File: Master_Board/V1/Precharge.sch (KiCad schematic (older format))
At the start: 24 parts, among them J701 649002227222, J702 649002227222, Q701 BC849BLT1G, Q702 BC849BLT1G, U701 LTV-816S, U702 LTV-816S

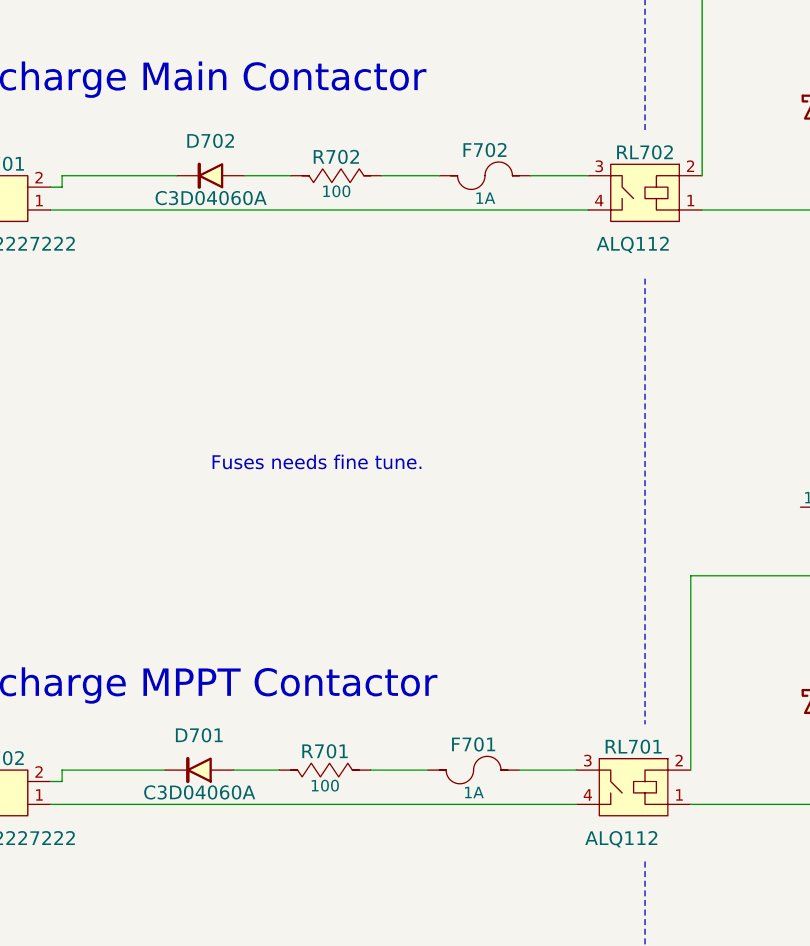
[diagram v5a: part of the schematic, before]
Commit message: Create Master board PCB
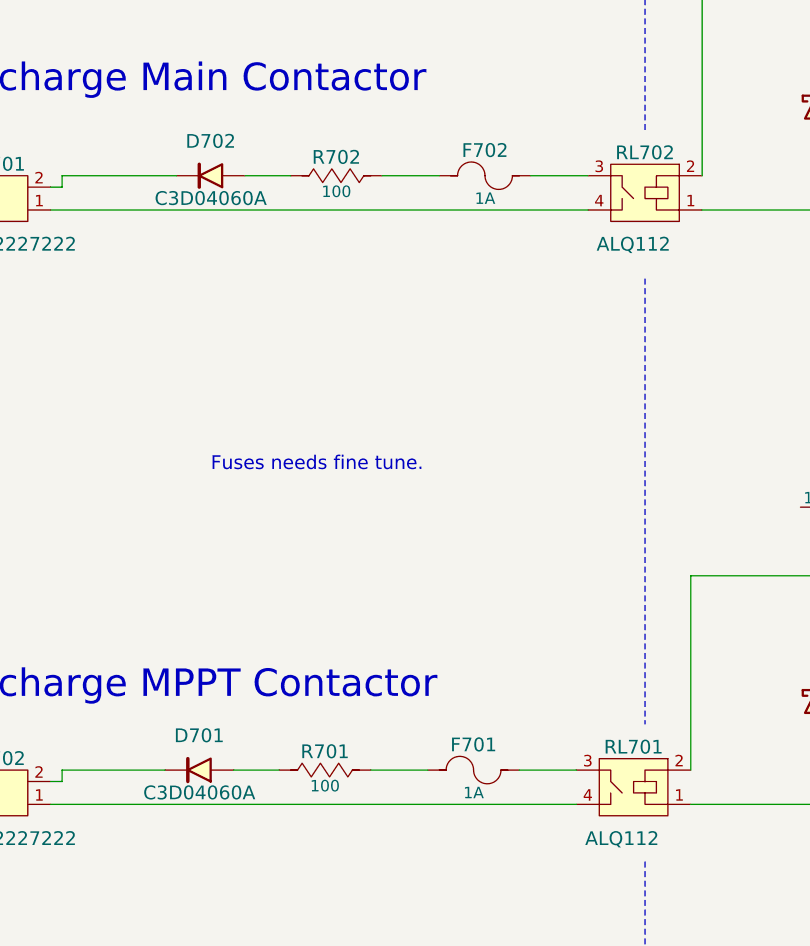
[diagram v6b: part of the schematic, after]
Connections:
- net at RL702.3: now also F702.2; no longer F702.1
- net at R702.1: now also D702.2 (Anode); no longer F702.2
- net at R702.2: now also F702.1; no longer D702.2 (Anode)
- net at RL701.3: now also F701.2; no longer F701.1
- net at R701.1: now also D701.2 (Anode); no longer F701.2
- net at R701.2: now also F701.1; no longer D701.2 (Anode)
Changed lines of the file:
@@
 	5300 4600 5300 4550
-$Comp
-L 39511000440 F702
-U 1 1 5945789A
-P 3050 2350
-F 0 "F702" H 3050 2460 60  0000 C CNN
-F 1 "39511000440" H 3050 2050 50  0001 C CNN
-F 2 "Fuses:TE5_395" H 3050 1450 30  0001 C CNN
-F 3 "http://www.littelfuse.com/~/media/electronics/datasheets/fuses/littelfuse_fuse_395_datasheet.pdf.pdf" H 3050 1400 30  0001 C CNN
-F 4 "Digikey" H 3050 1150 60  0001 C CNN "Supplier"
-F 5 "WK0009-ND" H 3050 1050 60  0001 C CNN "Supplier Part Number"
-F 6 "Littelfuse Inc." H 3050 900 60  0001 C CNN "Manufacturer"
-F 7 "56200001009" H 3050 750 60  0001 C CNN "Manufacturer Part Number"
-F 8 "FUSE HOLDER RADIAL 250V 6.3A PCB" H 3050 600 60  0001 C CNN "Description"
-F 9 "1A" H 3050 2250 50  0000 C CNN "Current Rating (A)"
-F 10 "-" H 2950 2150 50  0001 C CNN "Voltage Rating - DC"
-F 11 "125V" H 3150 2150 60  0001 C CNN "Voltage Rating - AC"
-F 12 "Fuse Holder" H 3050 1250 60  0001 C CNN "Fuse Holder"
-	1    3050 2350
-	-1   0    0    -1
-$EndComp
 $Comp
 L 649002227222 J701
@@
 Wire Wire Line
 	3500 2350 3250 2350
-$Comp
-L TR50JBC100R R702
-U 1 1 59458C40
-P 2400 2350
-F 0 "R702" H 2400 2430 60  0000 C CNN
-F 1 "TR50JBC100R" H 2400 2050 50  0001 C CNN
-F 2 "Resistors:TR50" H 2400 1450 30  0001 C CNN
-F 3 "https://www.seielect.com/Catalog/SEI-tr.pdf" H 2400 1400 30  0001 C CNN
-F 4 "Digikey" H 2400 1950 60  0001 C CNN "Supplier"
-F 5 "TR50JBC100R-ND" H 2400 1850 60  0001 C CNN "Supplier Part Number"
-F 6 "Stackpole Electronics Inc." H 2400 1750 60  0001 C CNN "Manufacturer"
-F 7 "TR50JBC100R" H 2400 1650 60  0001 C CNN "Manufacturer Part Number"
-F 8 "RES 100 OHM 50W 5% TO220" H 2400 1550 60  0001 C CNN "Description"
-F 9 "100" H 2400 2280 50  0000 C CNN "Resistance (Ohms)"
-F 10 "±5%" H 2810 2270 50  0001 C CNN "Tolerance (%)"
-F 11 "50W" H 2400 2210 50  0001 C CNN "Puissance (Watts)"
-	1    2400 2350
-	-1   0    0    -1
-$EndComp
 Wire Wire Line
 	2850 2350 2600 2350
 Wire Wire Line
 	2200 2350 2000 2350
-$Comp
-L 39511000440 F701
-U 1 1 59458F9F
-P 3000 4950
-F 0 "F701" H 3000 5060 60  0000 C CNN
-F 1 "39511000440" H 3000 4650 50  0001 C CNN
-F 2 "Fuses:TE5_395" H 3000 4050 30  0001 C CNN
-F 3 "http://www.littelfuse.com/~/media/electronics/datasheets/fuses/littelfuse_fuse_395_datasheet.pdf.pdf" H 3000 4000 30  0001 C CNN
-F 4 "Digikey" H 3000 3750 60  0001 C CNN "Supplier"
-F 5 "WK0009-ND" H 3000 3650 60  0001 C CNN "Supplier Part Number"
-F 6 "Littelfuse Inc." H 3000 3500 60  0001 C CNN "Manufacturer"
-F 7 "56200001009" H 3000 3350 60  0001 C CNN "Manufacturer Part Number"
-F 8 "FUSE HOLDER RADIAL 250V 6.3A PCB" H 3000 3200 60  0001 C CNN "Description"
-F 9 "1A" H 3000 4850 50  0000 C CNN "Current Rating (A)"
-F 10 "-" H 2900 4750 50  0001 C CNN "Voltage Rating - DC"
-F 11 "125V" H 3100 4750 60  0001 C CNN "Voltage Rating - AC"
-F 12 "Fuse Holder" H 3000 3850 60  0001 C CNN "Fuse Holder"
-	1    3000 4950
-	-1   0    0    -1
-$EndComp
 $Comp
 L 649002227222 J702
@@
 Wire Wire Line
 	3450 4950 3200 4950
-$Comp
-L TR50JBC100R R701
-U 1 1 59458FBA
-P 2350 4950
-F 0 "R701" H 2350 5030 60  0000 C CNN
-F 1 "TR50JBC100R" H 2350 4650 50  0001 C CNN
-F 2 "Resistors:TR50" H 2350 4050 30  0001 C CNN
-F 3 "https://www.seielect.com/Catalog/SEI-tr.pdf" H 2350 4000 30  0001 C CNN
-F 4 "Digikey" H 2350 4550 60  0001 C CNN "Supplier"
-F 5 "TR50JBC100R-ND" H 2350 4450 60  0001 C CNN "Supplier Part Number"
-F 6 "Stackpole Electronics Inc." H 2350 4350 60  0001 C CNN "Manufacturer"
-F 7 "TR50JBC100R" H 2350 4250 60  0001 C CNN "Manufacturer Part Number"
-F 8 "RES 100 OHM 50W 5% TO220" H 2350 4150 60  0001 C CNN "Description"
-F 9 "100" H 2350 4880 50  0000 C CNN "Resistance (Ohms)"
-F 10 "±5%" H 2760 4870 50  0001 C CNN "Tolerance (%)"
-F 11 "50W" H 2350 4810 50  0001 C CNN "Puissance (Watts)"
-	1    2350 4950
-	-1   0    0    -1
-$EndComp
 Wire Wire Line
 	2800 4950 2550 4950
@@
 	-1   0    0    -1
 $EndComp
+$Comp
+L 39511000440 F701
+U 1 1 59621787
+P 3000 4950
+F 0 "F701" H 3000 5060 60  0000 C CNN
+F 1 "39511000440" H 3000 4650 50  0001 C CNN
+F 2 "Fuses:TE5_395" H 3000 4050 30  0001 C CNN
+F 3 "http://www.littelfuse.com/~/media/electronics/datasheets/fuses/littelfuse_fuse_395_datasheet.pdf.pdf" H 3000 4000 30  0001 C CNN
+F 4 "Digikey" H 3000 3750 60  0001 C CNN "Supplier"
+F 5 "WK0009-ND" H 3000 3650 60  0001 C CNN "Supplier Part Number"
+F 6 "Littelfuse Inc." H 3000 3500 60  0001 C CNN "Manufacturer"
+F 7 "56200001009" H 3000 3350 60  0001 C CNN "Manufacturer Part Number"
+F 8 "FUSE HOLDER RADIAL 250V 6.3A PCB" H 3000 3200 60  0001 C CNN "Description"
+F 9 "1A" H 3000 4850 50  0000 C CNN "Current Rating (A)"
+F 10 "-" H 2900 4750 50  0001 C CNN "Voltage Rating - DC"
+F 11 "125V" H 3100 4750 60  0001 C CNN "Voltage Rating - AC"
+F 12 "Fuse Holder" H 3000 3850 60  0001 C CNN "Fuse Holder"
+	1    3000 4950
+	1    0    0    -1
+$EndComp
+$Comp
+L 39511000440 F702
+U 1 1 59621E4D
+P 3050 2350
+F 0 "F702" H 3050 2460 60  0000 C CNN
+F 1 "39511000440" H 3050 2050 50  0001 C CNN
+F 2 "Fuses:TE5_395" H 3050 1450 30  0001 C CNN
+F 3 "http://www.littelfuse.com/~/media/electronics/datasheets/fuses/littelfuse_fuse_395_datasheet.pdf.pdf" H 3050 1400 30  0001 C CNN
+F 4 "Digikey" H 3050 1150 60  0001 C CNN "Supplier"
+F 5 "WK0009-ND" H 3050 1050 60  0001 C CNN "Supplier Part Number"
+F 6 "Littelfuse Inc." H 3050 900 60  0001 C CNN "Manufacturer"
+F 7 "56200001009" H 3050 750 60  0001 C CNN "Manufacturer Part Number"
+F 8 "FUSE HOLDER RADIAL 250V 6.3A PCB" H 3050 600 60  0001 C CNN "Description"
+F 9 "1A" H 3050 2250 50  0000 C CNN "Current Rating (A)"
+F 10 "-" H 2950 2150 50  0001 C CNN "Voltage Rating - DC"
+F 11 "125V" H 3150 2150 60  0001 C CNN "Voltage Rating - AC"
+F 12 "Fuse Holder" H 3050 1250 60  0001 C CNN "Fuse Holder"
+	1    3050 2350
+	1    0    0    -1
+$EndComp
+$Comp
+L TR50JBC100R R702
+U 1 1 5963CF60
+P 2400 2350
+F 0 "R702" H 2400 2430 60  0000 C CNN
+F 1 "TR50JBC100R" H 2400 2050 50  0001 C CNN
+F 2 "Resistors:TR50" H 2400 1450 30  0001 C CNN
+F 3 "https://www.seielect.com/Catalog/SEI-tr.pdf" H 2400 1400 30  0001 C CNN
+F 4 "Digikey" H 2400 1950 60  0001 C CNN "Supplier"
+F 5 "TR50JBC100R-ND" H 2400 1850 60  0001 C CNN "Supplier Part Number"
+F 6 "Stackpole Electronics Inc." H 2400 1750 60  0001 C CNN "Manufacturer"
+F 7 "TR50JBC100R" H 2400 1650 60  0001 C CNN "Manufacturer Part Number"
+F 8 "RES 100 OHM 50W 5% TO220" H 2400 1550 60  0001 C CNN "Description"
+F 9 "100" H 2400 2280 50  0000 C CNN "Resistance (Ohms)"
+F 10 "±5%" H 2810 2270 50  0001 C CNN "Tolerance (%)"
+F 11 "50W" H 2400 2210 50  0001 C CNN "Puissance (Watts)"
+	1    2400 2350
+	1    0    0    -1
+$EndComp
+$Comp
+L TR50JBC100R R701
+U 1 1 5963D004
+P 2350 4950
+F 0 "R701" H 2350 5030 60  0000 C CNN
+F 1 "TR50JBC100R" H 2350 4650 50  0001 C CNN
+F 2 "Resistors:TR50" H 2350 4050 30  0001 C CNN
+F 3 "https://www.seielect.com/Catalog/SEI-tr.pdf" H 2350 4000 30  0001 C CNN
+F 4 "Digikey" H 2350 4550 60  0001 C CNN "Supplier"
+F 5 "TR50JBC100R-ND" H 2350 4450 60  0001 C CNN "Supplier Part Number"
+F 6 "Stackpole Electronics Inc." H 2350 4350 60  0001 C CNN "Manufacturer"
+F 7 "TR50JBC100R" H 2350 4250 60  0001 C CNN "Manufacturer Part Number"
+F 8 "RES 100 OHM 50W 5% TO220" H 2350 4150 60  0001 C CNN "Description"
+F 9 "100" H 2350 4880 50  0000 C CNN "Resistance (Ohms)"
+F 10 "±5%" H 2760 4870 50  0001 C CNN "Tolerance (%)"
+F 11 "50W" H 2350 4810 50  0001 C CNN "Puissance (Watts)"
+	1    2350 4950
+	1    0    0    -1
+$EndComp
 $EndSCHEMATC

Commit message: Routing BmsMasterBoard
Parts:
- removed R705, R706: RC0805JR-072K2L, Resistors:R0805, symbol RC0805JR-072K2L
- removed U701, U702: LTV-816S, IC:4-SMD, symbol LTV-816S-RESCUE-Master_Board
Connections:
- net at D703.2 (Anode), D705.1 (Cathode), RL702.1: now also Q702.3 (C)
- net at D704.2 (Anode), D706.1 (Cathode), RL701.1: now also Q701.3 (C)
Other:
- moved on the sheet: Q701, Q702, R707, R708
